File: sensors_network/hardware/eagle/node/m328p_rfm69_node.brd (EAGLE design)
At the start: 60.2 x 37.1 mm, 31 parts, among them IC2 L6920TSSOP8, U2 RFM69W, U3 ATMEGA328P, Y1 8MHz

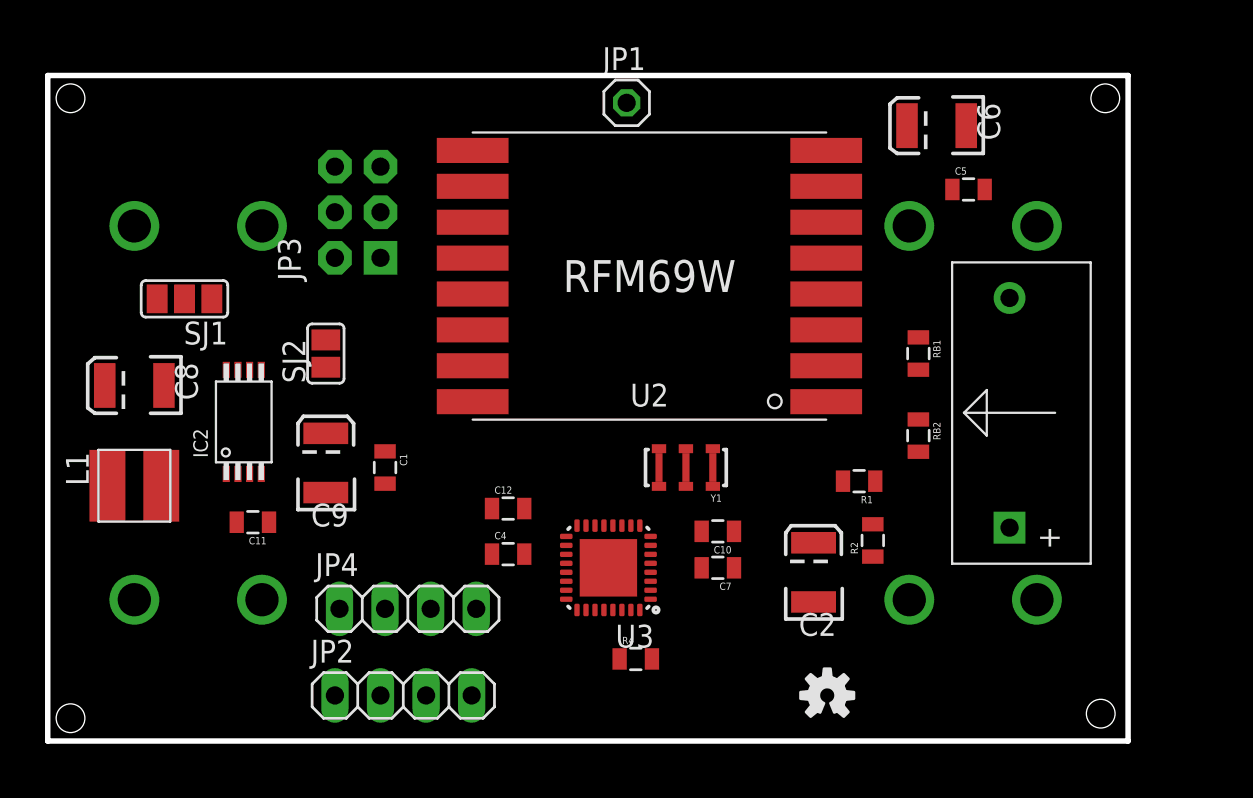
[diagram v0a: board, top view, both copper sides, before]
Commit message: [sensors network] Added sensor node eagle design - 2nd stage
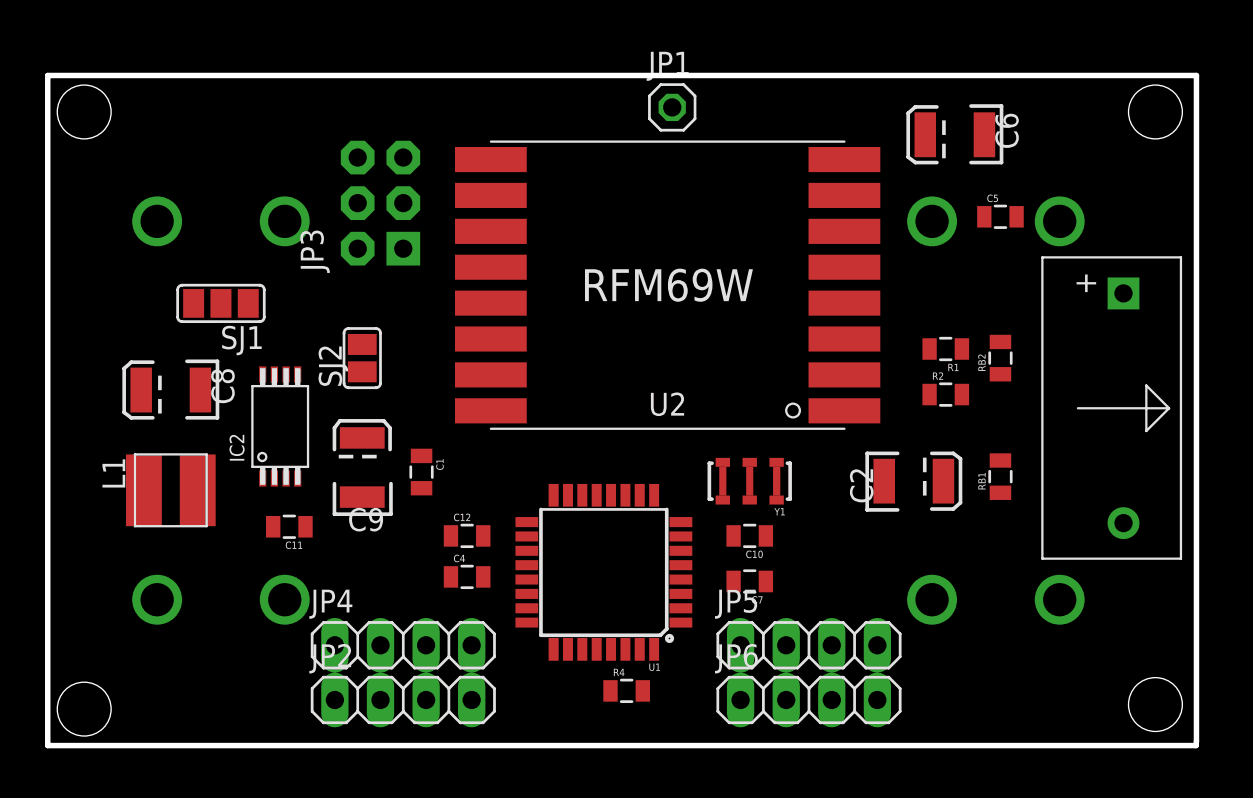
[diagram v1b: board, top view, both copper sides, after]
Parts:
- removed U$2: (no value), SparkFun-Aesthetics:OSHW-LOGO-S
- removed U3: ATMEGA328P, SparkFun-DigitalIC:MLF32-PAD
- added JP5, JP6: OTHER, pinhead:1X04
- added U1: ATMEGA328P_TQFP, SparkFun-DigitalIC:TQFP32-08
- moved R2 9.09 mm to (49.0, 19.3), turned to 0 degrees
- moved R1 8.81 mm to (49.0, 21.8)
- moved RB1 8.24 mm to (52.1, 14.7), turned to 90 degrees
- moved C2 7.55 mm to (47.2, 14.5), turned to 0 degrees
- moved CT1 6.36 mm to (58.9, 18.5), turned to 270 degrees
- moved RB2 6.29 mm to (52.1, 21.3), turned to 90 degrees
- moved Y1 3.64 mm to (38.1, 14.5)
- moved C12 2.75 mm to (22.4, 11.4)
- moved C4 2.62 mm to (22.4, 9.14)
- moved JP1 2.55 mm to (33.8, 35.3)
- moved C5 2.34 mm to (52.1, 29.2)
- moved SJ2 2.05 mm to (16.5, 21.3)
- moved C9 2.05 mm to (16.5, 15.2)
- moved IC2 2.05 mm to (11.9, 17.5)
- moved JP4 2.05 mm to (18.8, 5.33)
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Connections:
- new net B0: JP6.1, U1.30
- new net B1: JP6.2, U1.31
- new net D5: JP5.1, U1.1
- new net D6: JP5.2, U1.2
- net +3V3: now also JP5.4, JP6.4, U1.18, U1.4, U1.6; no longer U3.18, U3.4, U3.6
- net A0: now also U1.23; no longer U3.23
- net A1: now also U1.24; no longer U3.24
- net BATT_LVL: now also U1.25; no longer U3.25
- net CT_OUT: now also U1.26; no longer U3.26
- net GND: now also JP5.3, JP6.3, U1.21, U1.3, U1.5; no longer U3.21, U3.3, U3.5, U3.PAD
- net INT: now also U1.32; no longer U3.32
- net MISO: now also U1.16; no longer U3.16
- net MOSI: now also U1.15; no longer U3.15
- net N$12: now also U1.20; no longer U3.20
- net N$6: now also U1.8; no longer U3.8
- net N$9: now also U1.7; no longer U3.7
- net RESET: now also U1.29; no longer U3.29
- net SCK: now also U1.17; no longer U3.17
- net SCL: now also U1.28; no longer U3.28
- net SDA: now also U1.27; no longer U3.27
- net SS: now also U1.14; no longer U3.14
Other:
- board size 60.2 x 37.1 mm -> 64 x 37.3 mm

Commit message: [sensors network] Worked sensor node eagle design - 3rd stage
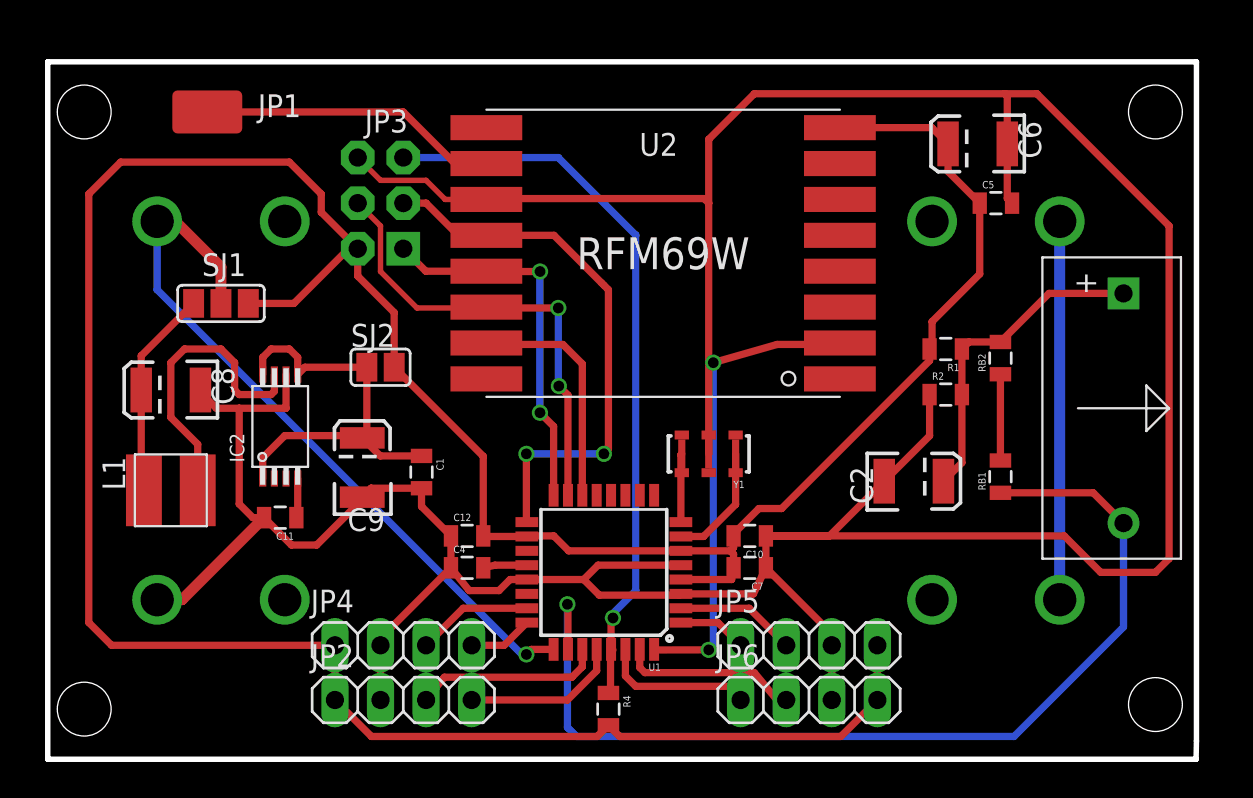
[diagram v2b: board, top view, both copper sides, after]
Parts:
- JP1: device pinhead:1X01 -> SparkFun-Connectors:LUXEON-PAD
- moved JP1 25.9 mm to (7.87, 35.1)
- moved Y1 2.75 mm to (35.8, 16.0)
- moved U2 1.80 mm to (33.3, 27.2)
- moved R4 1.44 mm to (30.2, 1.78), turned to 270 degrees
- moved C6 1.37 mm to (50.8, 33.3)
- moved SJ2 1.14 mm to (17.5, 20.8), turned to 0 degrees
- moved C5 0.80 mm to (51.8, 30.0)
- moved C7 0.76 mm to (38.1, 9.65)
- moved C11 0.72 mm to (11.9, 12.4)
- moved C4 0.51 mm to (22.4, 9.65)
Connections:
- net N$10: now also JP1.P$1; no longer JP1.1
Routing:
- net GND: track 0.00 -> 213.9 mm
- net +3V3: track 0.00 -> 176.2 mm
- net CT_OUT: track 0.00 -> 56.5 mm, vias 0 -> 1
- net RESET: track 0.00 -> 41.1 mm, vias 0 -> 1
- net BATT_LVL: track 0.00 -> 40.8 mm, vias 0 -> 1
- net SCK: track 0.00 -> 30.8 mm, vias 0 -> 2
- net INT: track 0.00 -> 26.4 mm, vias 0 -> 2
- net MOSI: track 0.00 -> 25.8 mm, vias 0 -> 2
- net N$7: track 0.00 -> 23.3 mm
- net N$8: track 0.00 -> 21.1 mm
- net MISO: track 0.00 -> 20.9 mm, vias 0 -> 2
- net N$11: track 0.00 -> 18.1 mm
- net N$1: track 0.00 -> 16.8 mm
- net N$10: track 0.00 -> 16.7 mm
- net SS: track 0.00 -> 13.2 mm
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- added copper zone on layer 1, net GND
- added copper zone on layer 16, net GND
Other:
- board size 64 x 37.3 mm -> 64 x 38.9 mm

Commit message: [sensors network] Worked sensor node eagle design - 4th stage
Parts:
- IC2: value L6920TSSOP8 -> L6920
- JP3: value AVR_SPI_PRG_6NS -> ISP
- U1: value ATMEGA328P_TQFP -> M328P
- moved JP1 1.30 mm to (8.13, 36.3)
- moved BAT3 1.14 mm to (29.7, 30.0)
- moved C5 0.92 mm to (51.3, 30.7)
- moved JP4 0.80 mm to (19.6, 5.08)
- moved JP5 0.80 mm to (40.6, 5.08)
- moved C12 0.76 mm to (22.4, 12.2)
- moved C6 0.76 mm to (50.8, 34.0)
- moved JP2 0.76 mm to (19.6, 2.29)
- moved JP6 0.76 mm to (40.6, 2.29)
- moved CT1 0.76 mm to (58.9, 19.3)
- moved BAT4 0.72 mm to (29.7, 8.38)
- moved C10 0.51 mm to (38.1, 11.9)
- moved C4 0.51 mm to (22.4, 10.2)
- moved JP3 0.25 mm to (17.3, 30.0)
- moved C11 0.25 mm to (11.9, 12.2), turned to 270 degrees
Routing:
- net GND: track 213.9 -> 205.7 mm
- net BATT_LVL: track 40.8 -> 42.8 mm
- net INT: track 26.4 -> 25.1 mm
- net MOSI: track 25.8 -> 27.0 mm
- net B0: track 8.55 -> 7.54 mm
- net SDA: track 10.5 -> 9.68 mm
- net B1: track 10.0 -> 9.16 mm
- net SCL: track 8.83 -> 8.07 mm
- net D5: track 3.85 -> 3.19 mm
- net A0: track 6.47 -> 5.81 mm
- net D6: track 6.72 -> 6.07 mm
- net A1: track 3.60 -> 2.94 mm
- net +3V3: track 176.2 -> 176.7 mm
- net N$8: track 21.1 -> 21.6 mm
- removed copper zone on layer 16, net GND
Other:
- board size 64 x 38.9 mm -> 64 x 39.9 mm
- board text added: "+3V3 GND A0 A1"
- board text added: "+3V3 GND SDA SCL"
- board text added: "B0 B1 GND +3V3"
- board text added: "D5 D6 GND +3V3"
- board text added: "VB_EN"
- board text added: "VB_EN | VB_DIS"

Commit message: [sensors network] Worked sensor node eagle design - 5th stage
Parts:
- JP1: value ANT -> ANTENNA
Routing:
- net RESET: track 41.4 -> 35.0 mm
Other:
- board text added: "Antenna Length: 433 MHz -> 165 mm 868 MHz -> 82 mm 915 MHz -> 78 mm"
- board text added: "Current Transformer 5A max"
- board text added: "MySensors RFM69 Node"
- board text added: "TT"

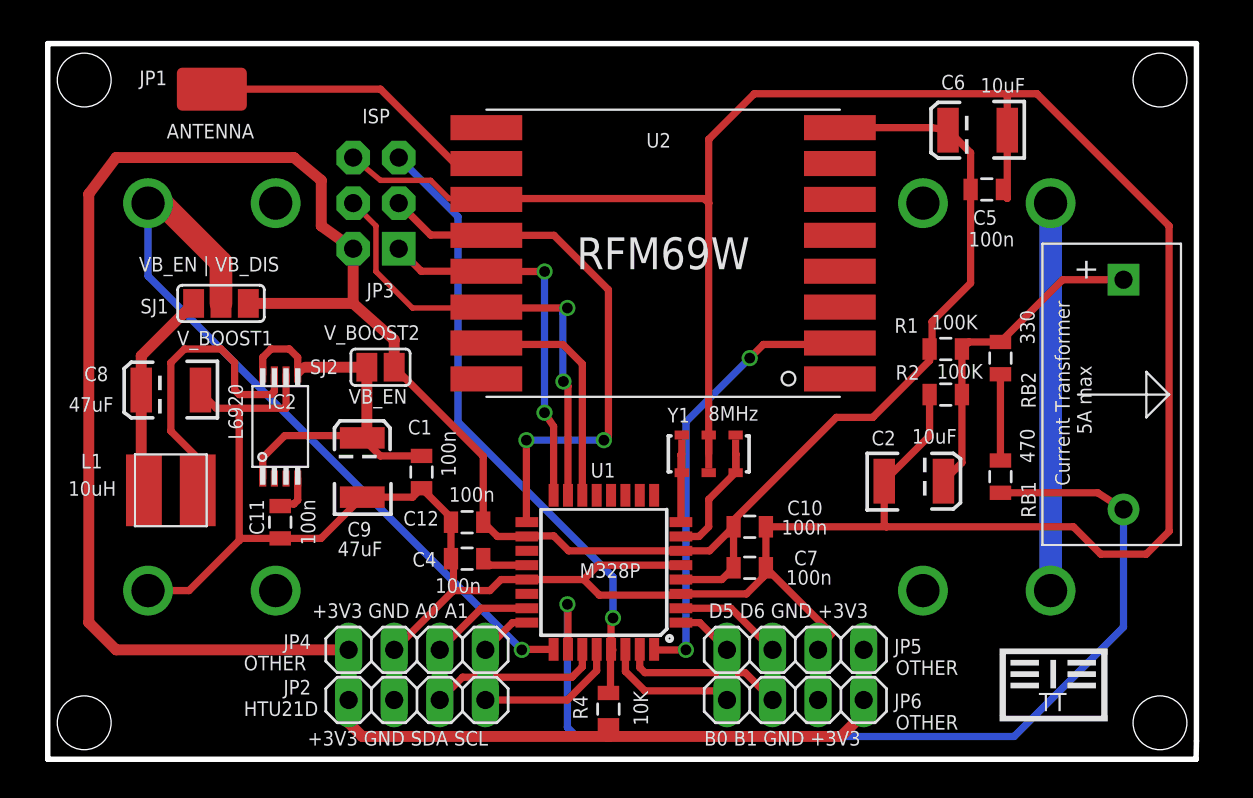
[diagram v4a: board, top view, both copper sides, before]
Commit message: [sensors network] moved ct to the outside a little bit as it interfered with the battery support
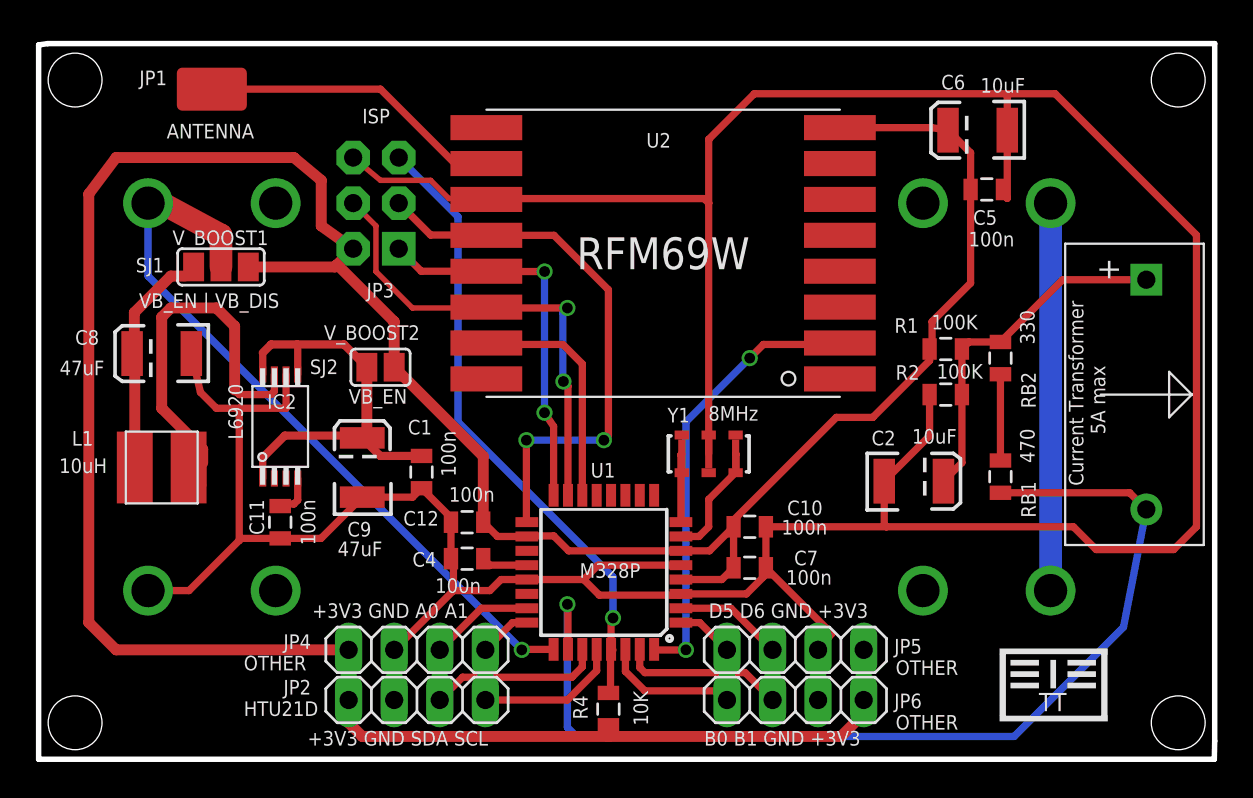
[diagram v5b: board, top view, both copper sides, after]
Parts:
- moved C8 2.09 mm to (5.33, 21.6)
- moved SJ1 2.03 mm to (8.64, 26.4)
- moved L1 1.37 mm to (5.33, 15.2)
- moved CT1 1.27 mm to (60.2, 19.3)
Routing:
- net N$1: track 17.0 -> 23.2 mm
- net GND: track 205.8 -> 210.2 mm
- net N$2: track 11.7 -> 13.6 mm
- net CT_OUT: track 56.8 -> 58.3 mm
- net BATT_LVL: track 43.0 -> 41.6 mm
- net N$11: track 18.4 -> 19.7 mm
- net N$7: track 23.3 -> 24.4 mm
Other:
- board size 64 x 39.9 mm -> 65.5 x 39.9 mm
